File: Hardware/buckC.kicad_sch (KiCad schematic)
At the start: 31 parts, among them U6 SiC437BED-T1-GE3

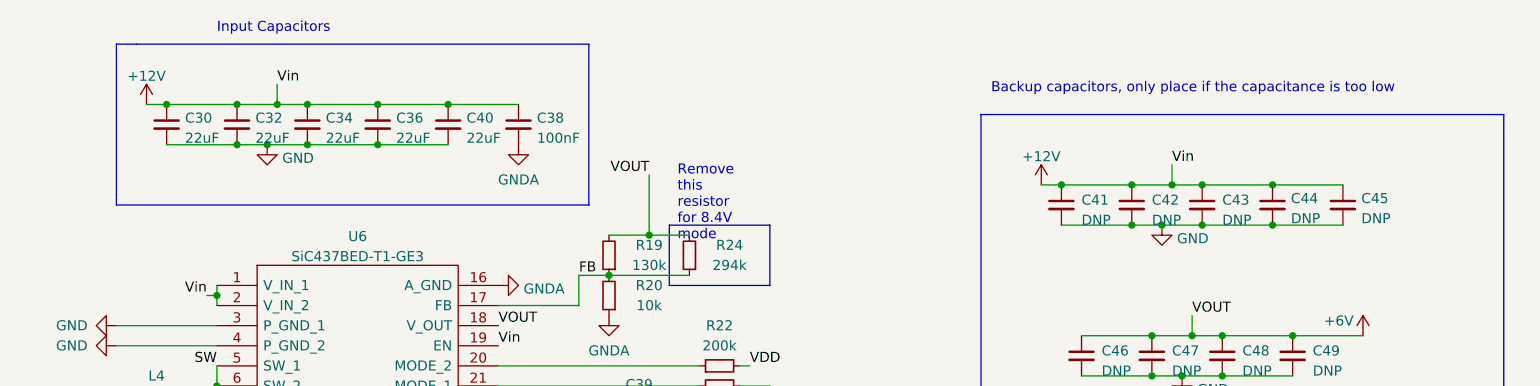
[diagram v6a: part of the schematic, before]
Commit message: changed some caps, added gerbers and bom
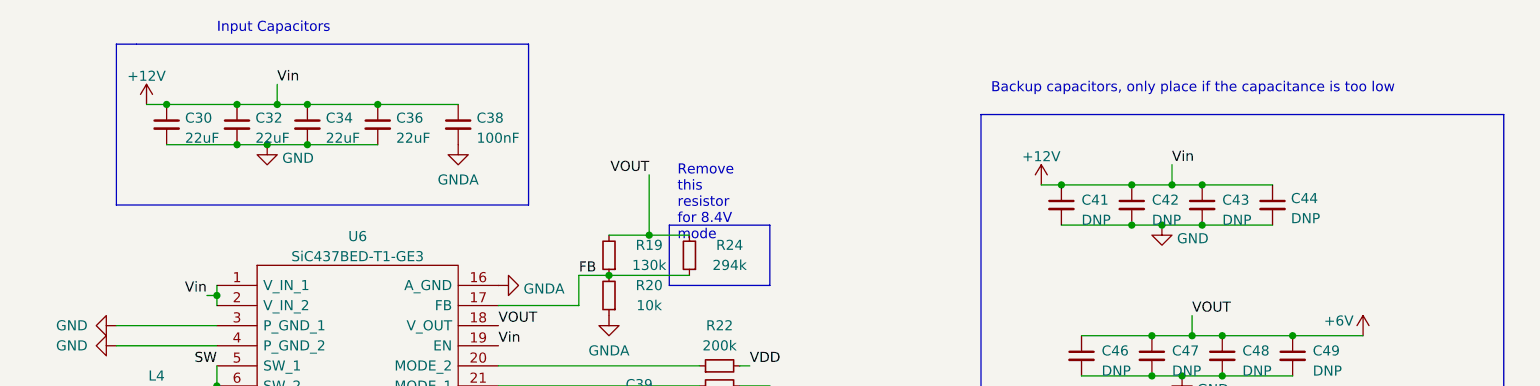
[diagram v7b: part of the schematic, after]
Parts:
- removed C40: 22uF, Capacitor_SMD:C_0805_2012Metric, symbol Device:C_Small
- removed C45: DNP, Capacitor_SMD:C_0805_2012Metric, symbol Device:C_Small
- C30, C32, C33, C34, C35, C36, C37, C41, C42, C43, C44, C47, C49: footprint Capacitor_SMD:C_0805_2012Metric -> Capacitor_SMD:C_1206_3216Metric
- R18, R19, R20, R22, R23, R24: footprint Capacitor_SMD:C_0402_1005Metric -> Resistor_SMD:R_0402_1005Metric
- R21: footprint Capacitor_SMD:C_0603_1608Metric -> Resistor_SMD:R_0603_1608Metric
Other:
- moved on the sheet: C38

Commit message: review changes + some new features
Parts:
- added C40: DNP, Capacitor_SMD:C_1206_3216Metric, symbol Device:C_Small
- added Q1: SSM3K15AMFV,L3F, Package_TO_SOT_SMD:SOT-723, symbol Device:Q_NMOS_GSD
- added R38: 10k, Resistor_SMD:R_0402_1005Metric, symbol Device:R_Small
- added R39: 1k, Resistor_SMD:R_0402_1005Metric, symbol Device:R_Small
- C30, C32, C33, C35, C37: value 22uF -> 47uF
- C31: value 22uF -> DNP; footprint Capacitor_SMD:C_0805_2012Metric -> Capacitor_SMD:C_1206_3216Metric
- C34, C36: value 22uF -> DNP
- R21: footprint Resistor_SMD:R_0603_1608Metric -> Resistor_SMD:R_0402_1005Metric
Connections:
- net +12V: now also R38.2; no longer U6.19 (EN)
- net +6V: now also C40.1
- net GND: now also C40.2, Q1.2 (S), R39.1
- new net BUCK_EN: Q1.1 (G), R39.2
- new net EN: Q1.3 (D), R38.1, U6.19 (EN)
